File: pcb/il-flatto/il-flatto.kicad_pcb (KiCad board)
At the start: 2 copper layers, 88.3 x 63.5 mm, 52 parts, among them IC1 ATmega1284P-P, IC2 MCP1825S, IC3 MAX1811, Q1 12MHz, X2 SD_Card

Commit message: good to go?
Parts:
- removed - +: BAT, Connector_JST:JST_PH_B2B-PH-K_1x02_P2.00mm_Vertical
- removed the ? at (228.0, 128.3)
- removed the ? at (148.6, 128.3)
- removed the ? at (148.6, 73.7)
- removed the C1 at (176.5, 111.8)
- removed the C2 at (176.5, 95.2)
- removed the C3 at (168.9, 91.4)
- removed the C4 at (158.7, 89.5)
- removed the C5 at (174.0, 82.5)
- removed the C6 at (174.0, 89.5)
- removed the D1 at (165.7, 118.1)
- removed the G*** at (193.5, 101.0)
- removed the G*** at (188.1, 100.8)
- removed ISP: ISP, footprints:PinSocket_2x03_P2.54mm zero footprint mirror
- removed JTAG: JTAG, footprints:PinSocket_2x05_P2.54mm zero footprint mirror
- removed the Q1 at (175.3, 101.1)
- removed the R1 at (160.7, 99.7)
- removed the R10 at (209.6, 120.7)
- removed the R11 at (200.7, 117.5)
- removed the R2 at (170.8, 103.5)
- removed the R3 at (170.8, 107.3)
- removed the R4 at (170.8, 111.1)
- removed the R5 at (160.7, 95.9)
- removed the R6 at (219.7, 81.3)
- removed the R7 at (200.7, 84.5)
- removed the R8 at (218.4, 117.5)
- removed the R9 at (228.6, 84.5)
- removed the REF** at (228.0, 73.7)
- removed Reset: SW_SPST, Button_Switch_THT:SW_PUSH_6mm
- removed the SV1(A)1 at (216.5, 74.9)
- removed the SV2(B)1 at (170.2, 75.0)
- removed the SV3(C)1 at (205.8, 127.0)
- removed the SV4(D)1 at (160.1, 127.0)
- removed Se100: S1, footprints:EG1218
- added ?: , , F.Cu at (242.6, 83.3)
- added ?: , , F.Cu at (242.6, 154.3)
- added ?: , , F.Cu at (163.2, 28.6)
- added ?: , , F.Cu at (163.2, 99.7)
- added ?: , , F.Cu at (163.2, 154.3)
- added ?: , , F.Cu at (163.2, 83.3)
- added ?: ATmega1284P-P, Package_DIP:DIP-40_W15.24mm, F.Cu at (195.2, 102.8)
- added C1: 22pf, Capacitor_THT:C_Disc_D3.8mm_W2.6mm_P2.50mm, F.Cu at (191.1, 137.8)
- added C1: 22pf, Capacitor_THT:C_Disc_D3.8mm_W2.6mm_P2.50mm, F.Cu at (191.1, 66.7)
- added C101: 22pf, Capacitor_SMD:C_0402_1005Metric, F.Cu at (192.3, 132.3)
- added C102: 22pf, Capacitor_SMD:C_0402_1005Metric, F.Cu at (192.4, 126.9)
- added C103: 100nf, Capacitor_SMD:C_0402_1005Metric, F.Cu at (193.5, 125.0)
- added C104: 10uf, Capacitor_SMD:C_0402_1005Metric, F.Cu at (172.3, 117.5)
- added C105: 10uf, Capacitor_SMD:C_0402_1005Metric, F.Cu at (189.6, 110.5)
- added C106: 10uf, Capacitor_SMD:C_0402_1005Metric, F.Cu at (189.9, 113.7)
- added C107: 10uf, Capacitor_SMD:C_0402_1005Metric, F.Cu at (217.8, 99.7)
- added C108: 10uf, Capacitor_SMD:C_0402_1005Metric, F.Cu at (170.8, 99.7)
- added C109: 10uf, Capacitor_SMD:C_0402_1005Metric, F.Cu at (234.3, 154.3)
- added C110: 10uf, Capacitor_SMD:C_0402_1005Metric, F.Cu at (188.6, 154.3)
- added C111: 100nf, Capacitor_SMD:C_0402_1005Metric, F.Cu at (216.6, 99.7)
- added C112: 100nf, Capacitor_SMD:C_0402_1005Metric, F.Cu at (172.1, 99.7)
- added C113: 100nf, Capacitor_SMD:C_0402_1005Metric, F.Cu at (187.3, 154.3)
- added C114: 100nf, Capacitor_SMD:C_0402_1005Metric, F.Cu at (233.0, 154.3)
- added C2: 22pf, Capacitor_THT:C_Disc_D3.8mm_W2.6mm_P2.50mm, F.Cu at (191.1, 121.3)
- added C2: 22pf, Capacitor_THT:C_Disc_D3.8mm_W2.6mm_P2.50mm, F.Cu at (191.1, 50.2)
- added C205: 100nf, Capacitor_SMD:C_0402_1005Metric, F.Cu at (209.0, 126.8)
- added C206: 100nf, Capacitor_SMD:C_0402_1005Metric, F.Cu at (209.0, 124.8)
- added C3: 100nf, Capacitor_THT:C_Disc_D7.0mm_W2.5mm_P5.00mm, F.Cu at (183.5, 46.4)
- added C3: 100nf, Capacitor_THT:C_Disc_D7.0mm_W2.5mm_P5.00mm, F.Cu at (183.5, 117.5)
- added C300: 10u, Capacitor_SMD:C_0603_1608Metric, F.Cu at (241.7, 141.0)
- added C301: 10u, Capacitor_SMD:C_0603_1608Metric, F.Cu at (217.8, 137.0)
- added C302: 10u, Capacitor_SMD:C_0603_1608Metric, F.Cu at (241.7, 132.8)
- added C303: 10u, Capacitor_SMD:C_0603_1608Metric, F.Cu at (217.8, 128.9)
- added C304: 10u, Capacitor_SMD:C_0603_1608Metric, F.Cu at (241.7, 124.9)
- added C305: 10u, Capacitor_SMD:C_0603_1608Metric, F.Cu at (217.8, 121.0)
- added C306: 10u, Capacitor_SMD:C_0603_1608Metric, F.Cu at (241.7, 116.9)
- added C307: 10u, Capacitor_SMD:C_0603_1608Metric, F.Cu at (217.8, 112.9)
- added C4: 10uf, Capacitor_THT:CP_Radial_D5.0mm_P2.00mm, F.Cu at (173.3, 115.6)
- added C4: 10uf, Capacitor_THT:CP_Radial_D5.0mm_P2.00mm, F.Cu at (173.3, 44.5)
- added C5: 10uf, Capacitor_THT:CP_Radial_D5.0mm_P2.00mm, F.Cu at (188.6, 108.6)
- added C5: 10uf, Capacitor_THT:CP_Radial_D5.0mm_P2.00mm, F.Cu at (188.6, 37.5)
- added C6: 100uf, Capacitor_THT:CP_Radial_D5.0mm_P2.00mm, F.Cu at (188.6, 44.5)
- added C6: 100uf, Capacitor_THT:CP_Radial_D5.0mm_P2.00mm, F.Cu at (188.6, 115.6)
- added D1: LED, LED_THT:LED_D3.0mm, F.Cu at (180.3, 73.1)
- added D1: LED, LED_THT:LED_D3.0mm, F.Cu at (180.3, 144.1)
- added D101: LED, LED_SMD:LED_0603_1608Metric, F.Cu at (181.6, 142.2)
- added D102: CHRG, LED_SMD:LED_0603_1608Metric, F.Cu at (168.9, 117.5)
- added D200: SMD-LX0707RGB-TR, footprints:SMD-LX0707RGB-TR, F.Cu at (215.7, 141.0)
- added D201: SMD-LX0707RGB-TR, footprints:SMD-LX0707RGB-TR, F.Cu at (219.7, 141.0)
- added D202: SMD-LX0707RGB-TR, footprints:SMD-LX0707RGB-TR, F.Cu at (223.7, 141.0)
- added D203: SMD-LX0707RGB-TR, footprints:SMD-LX0707RGB-TR, F.Cu at (227.7, 141.0)
- added D204: SMD-LX0707RGB-TR, footprints:SMD-LX0707RGB-TR, F.Cu at (231.7, 141.0)
- added D205: SMD-LX0707RGB-TR, footprints:SMD-LX0707RGB-TR, F.Cu at (235.7, 141.0)
- added D206: SMD-LX0707RGB-TR, footprints:SMD-LX0707RGB-TR, F.Cu at (239.7, 141.0)
- added D207: SMD-LX0707RGB-TR, footprints:SMD-LX0707RGB-TR, F.Cu at (243.7, 141.0)
- added D208: SMD-LX0707RGB-TR, footprints:SMD-LX0707RGB-TR, F.Cu at (243.7, 137.0)
- added D209: SMD-LX0707RGB-TR, footprints:SMD-LX0707RGB-TR, F.Cu at (239.7, 137.0)
- added D210: SMD-LX0707RGB-TR, footprints:SMD-LX0707RGB-TR, F.Cu at (235.7, 137.0)
- added D211: SMD-LX0707RGB-TR, footprints:SMD-LX0707RGB-TR, F.Cu at (231.7, 137.0)
- added D212: SMD-LX0707RGB-TR, footprints:SMD-LX0707RGB-TR, F.Cu at (227.7, 137.0)
- added D213: SMD-LX0707RGB-TR, footprints:SMD-LX0707RGB-TR, F.Cu at (223.7, 137.0)
- added D214: SMD-LX0707RGB-TR, footprints:SMD-LX0707RGB-TR, F.Cu at (219.7, 137.0)
- added D215: SMD-LX0707RGB-TR, footprints:SMD-LX0707RGB-TR, F.Cu at (215.7, 137.0)
- added D216: SMD-LX0707RGB-TR, footprints:SMD-LX0707RGB-TR, F.Cu at (215.7, 133.0)
- added D217: SMD-LX0707RGB-TR, footprints:SMD-LX0707RGB-TR, F.Cu at (219.7, 133.0)
- added D218: SMD-LX0707RGB-TR, footprints:SMD-LX0707RGB-TR, F.Cu at (223.7, 133.0)
- added D219: SMD-LX0707RGB-TR, footprints:SMD-LX0707RGB-TR, F.Cu at (227.7, 133.0)
- added D220: SMD-LX0707RGB-TR, footprints:SMD-LX0707RGB-TR, F.Cu at (231.7, 133.0)
- added D221: SMD-LX0707RGB-TR, footprints:SMD-LX0707RGB-TR, F.Cu at (235.7, 133.0)
- added D222: SMD-LX0707RGB-TR, footprints:SMD-LX0707RGB-TR, F.Cu at (239.7, 133.0)
- added D223: SMD-LX0707RGB-TR, footprints:SMD-LX0707RGB-TR, F.Cu at (243.7, 133.0)
- added D224: SMD-LX0707RGB-TR, footprints:SMD-LX0707RGB-TR, F.Cu at (243.7, 129.0)
- added D225: SMD-LX0707RGB-TR, footprints:SMD-LX0707RGB-TR, F.Cu at (239.7, 129.0)
- added D226: SMD-LX0707RGB-TR, footprints:SMD-LX0707RGB-TR, F.Cu at (235.7, 129.0)
- added D227: SMD-LX0707RGB-TR, footprints:SMD-LX0707RGB-TR, F.Cu at (231.7, 129.0)
- added D228: SMD-LX0707RGB-TR, footprints:SMD-LX0707RGB-TR, F.Cu at (227.7, 129.0)
- added D229: SMD-LX0707RGB-TR, footprints:SMD-LX0707RGB-TR, F.Cu at (223.7, 129.0)
- added D230: SMD-LX0707RGB-TR, footprints:SMD-LX0707RGB-TR, F.Cu at (219.7, 129.0)
- added D231: SMD-LX0707RGB-TR, footprints:SMD-LX0707RGB-TR, F.Cu at (215.7, 129.0)
- added D232: SMD-LX0707RGB-TR, footprints:SMD-LX0707RGB-TR, F.Cu at (215.7, 125.0)
- added D233: SMD-LX0707RGB-TR, footprints:SMD-LX0707RGB-TR, F.Cu at (219.7, 125.0)
- added D234: SMD-LX0707RGB-TR, footprints:SMD-LX0707RGB-TR, F.Cu at (223.7, 125.0)
- added D235: SMD-LX0707RGB-TR, footprints:SMD-LX0707RGB-TR, F.Cu at (227.7, 125.0)
- added D236: SMD-LX0707RGB-TR, footprints:SMD-LX0707RGB-TR, F.Cu at (231.7, 125.0)
- added D237: SMD-LX0707RGB-TR, footprints:SMD-LX0707RGB-TR, F.Cu at (235.7, 125.0)
- added D238: SMD-LX0707RGB-TR, footprints:SMD-LX0707RGB-TR, F.Cu at (239.7, 125.0)
- added D239: SMD-LX0707RGB-TR, footprints:SMD-LX0707RGB-TR, F.Cu at (243.7, 125.0)
- added D240: SMD-LX0707RGB-TR, footprints:SMD-LX0707RGB-TR, F.Cu at (243.7, 121.0)
- added D241: SMD-LX0707RGB-TR, footprints:SMD-LX0707RGB-TR, F.Cu at (239.7, 121.0)
- added D242: SMD-LX0707RGB-TR, footprints:SMD-LX0707RGB-TR, F.Cu at (235.7, 121.0)
- added D243: SMD-LX0707RGB-TR, footprints:SMD-LX0707RGB-TR, F.Cu at (231.7, 121.0)
- added D244: SMD-LX0707RGB-TR, footprints:SMD-LX0707RGB-TR, F.Cu at (227.7, 121.0)
- added D245: SMD-LX0707RGB-TR, footprints:SMD-LX0707RGB-TR, F.Cu at (223.7, 121.0)
- added D246: SMD-LX0707RGB-TR, footprints:SMD-LX0707RGB-TR, F.Cu at (219.7, 121.0)
- added D247: SMD-LX0707RGB-TR, footprints:SMD-LX0707RGB-TR, F.Cu at (215.7, 121.0)
- added D248: SMD-LX0707RGB-TR, footprints:SMD-LX0707RGB-TR, F.Cu at (215.7, 117.0)
- added D249: SMD-LX0707RGB-TR, footprints:SMD-LX0707RGB-TR, F.Cu at (219.7, 117.0)
- added D250: SMD-LX0707RGB-TR, footprints:SMD-LX0707RGB-TR, F.Cu at (223.7, 117.0)
- added D251: SMD-LX0707RGB-TR, footprints:SMD-LX0707RGB-TR, F.Cu at (227.7, 117.0)
- added D252: SMD-LX0707RGB-TR, footprints:SMD-LX0707RGB-TR, F.Cu at (231.7, 117.0)
- added D253: SMD-LX0707RGB-TR, footprints:SMD-LX0707RGB-TR, F.Cu at (235.7, 117.0)
- added D254: SMD-LX0707RGB-TR, footprints:SMD-LX0707RGB-TR, F.Cu at (239.7, 117.0)
- added D255: SMD-LX0707RGB-TR, footprints:SMD-LX0707RGB-TR, F.Cu at (243.7, 117.0)
- added D256: SMD-LX0707RGB-TR, footprints:SMD-LX0707RGB-TR, F.Cu at (243.7, 113.0)
- added D257: SMD-LX0707RGB-TR, footprints:SMD-LX0707RGB-TR, F.Cu at (239.7, 113.0)
- added D258: SMD-LX0707RGB-TR, footprints:SMD-LX0707RGB-TR, F.Cu at (235.7, 113.0)
- added D259: SMD-LX0707RGB-TR, footprints:SMD-LX0707RGB-TR, F.Cu at (231.7, 113.0)
- added D260: SMD-LX0707RGB-TR, footprints:SMD-LX0707RGB-TR, F.Cu at (227.7, 113.0)
- added D261: SMD-LX0707RGB-TR, footprints:SMD-LX0707RGB-TR, F.Cu at (223.7, 113.0)
- added D262: SMD-LX0707RGB-TR, footprints:SMD-LX0707RGB-TR, F.Cu at (219.7, 113.0)
- added D263: SMD-LX0707RGB-TR, footprints:SMD-LX0707RGB-TR, F.Cu at (215.7, 113.0)
- added J103: ISP, footprints:PinSocket_2x03_P2.54mm zero footprint mirror, F.Cu at (162.1, 113.7)
- added J105: JTAG, footprints:PinSocket_2x05_P2.54mm zero footprint mirror, F.Cu at (161.9, 145.4)
- added J3: ISP, footprints:PinSocket_2x03_P2.54mm zero footprint mirror, F.Cu at (162.1, 42.6)
- added J5: JTAG, footprints:PinSocket_2x05_P2.54mm zero footprint mirror, F.Cu at (161.9, 74.4)
- added JP103: Conn_01x03, footprints:PinHeader_1x03_P2.54mm zero footprint, F.Cu at (190.5, 146.7)
- added Q1: 12MHz, Crystal:Crystal_HC49-4H_Vertical, F.Cu at (189.9, 127.1)
- added Q1: 12MHz, Crystal:Crystal_HC49-4H_Vertical, F.Cu at (189.9, 56.0)
- added Q101: 12MHz, Crystal:Crystal_SMD_Abracon_ABM8G-4Pin_3.2x2.5mm, F.Cu at (192.3, 129.6)
- added R1: 68, Resistor_THT:R_Axial_DIN0207_L6.3mm_D2.5mm_P10.16mm_Horizontal, F.Cu at (175.3, 125.7)
- added R1: 68, Resistor_THT:R_Axial_DIN0207_L6.3mm_D2.5mm_P10.16mm_Horizontal, F.Cu at (175.3, 54.7)
- added R10: 68, Resistor_THT:R_Axial_DIN0207_L6.3mm_D2.5mm_P10.16mm_Horizontal, F.Cu at (224.2, 146.7)
- added R10: 68, Resistor_THT:R_Axial_DIN0207_L6.3mm_D2.5mm_P10.16mm_Horizontal, F.Cu at (224.2, 75.6)
- added R101: 68, Resistor_SMD:R_0402_1005Metric, F.Cu at (180.3, 125.1)
- added R102: 68, Resistor_SMD:R_0402_1005Metric, F.Cu at (180.3, 126.4)
- added R103: 1.5k, Resistor_SMD:R_0402_1005Metric, F.Cu at (178.4, 135.3)
- added R104: 220, Resistor_SMD:R_0402_1005Metric, F.Cu at (181.6, 141.0)
- added R105: 10k, Resistor_SMD:R_0402_1005Metric, F.Cu at (178.4, 140.3)
- added R106: 68, Resistor_SMD:R_0402_1005Metric, F.Cu at (229.4, 107.3)
- added R107: 68, Resistor_SMD:R_0402_1005Metric, F.Cu at (220.5, 110.5)
- added R108: 68, Resistor_SMD:R_0402_1005Metric, F.Cu at (238.3, 143.5)
- added R109: 68, Resistor_SMD:R_0402_1005Metric, F.Cu at (238.2, 110.5)
- added R11: 68, Resistor_THT:R_Axial_DIN0207_L6.3mm_D2.5mm_P10.16mm_Horizontal, F.Cu at (215.3, 72.5)
- added R11: 68, Resistor_THT:R_Axial_DIN0207_L6.3mm_D2.5mm_P10.16mm_Horizontal, F.Cu at (215.3, 143.5)
- added R110: 68, Resistor_SMD:R_0402_1005Metric, F.Cu at (229.5, 146.7)
- added R111: 68, Resistor_SMD:R_0402_1005Metric, F.Cu at (220.5, 143.5)
- added R112: 470, Resistor_SMD:R_0402_1005Metric, F.Cu at (168.9, 114.9)
- added R2: 68, Resistor_THT:R_Axial_DIN0207_L6.3mm_D2.5mm_P10.16mm_Horizontal, F.Cu at (185.4, 129.5)
- added R2: 68, Resistor_THT:R_Axial_DIN0207_L6.3mm_D2.5mm_P10.16mm_Horizontal, F.Cu at (185.4, 58.5)
- added R201: 5.1k, Resistor_SMD:R_0402_1005Metric, F.Cu at (165.7, 117.5)
- added R202: 5.1k, Resistor_SMD:R_0402_1005Metric, F.Cu at (167.0, 132.1)
- added R203: 2.5k, Resistor_SMD:R_0402_1005Metric, F.Cu at (177.8, 132.7)
- added R204: 10k, Resistor_SMD:R_0402_1005Metric, F.Cu at (179.1, 132.7)
- added R3: 1.5k, Resistor_THT:R_Axial_DIN0207_L6.3mm_D2.5mm_P10.16mm_Horizontal, F.Cu at (185.4, 133.3)
- added R3: 1.5k, Resistor_THT:R_Axial_DIN0207_L6.3mm_D2.5mm_P10.16mm_Horizontal, F.Cu at (185.4, 62.3)
- added R4: 220, Resistor_THT:R_Axial_DIN0207_L6.3mm_D2.5mm_P10.16mm_Horizontal, F.Cu at (185.4, 137.2)
- added R4: 220, Resistor_THT:R_Axial_DIN0207_L6.3mm_D2.5mm_P10.16mm_Horizontal, F.Cu at (185.4, 66.1)
- added R5: 10k, Resistor_THT:R_Axial_DIN0207_L6.3mm_D2.5mm_P10.16mm_Horizontal, F.Cu at (175.3, 50.9)
- added R5: 10k, Resistor_THT:R_Axial_DIN0207_L6.3mm_D2.5mm_P10.16mm_Horizontal, F.Cu at (175.3, 121.9)
- added R6: 68, Resistor_THT:R_Axial_DIN0207_L6.3mm_D2.5mm_P10.16mm_Horizontal, F.Cu at (234.3, 36.3)
- added R6: 68, Resistor_THT:R_Axial_DIN0207_L6.3mm_D2.5mm_P10.16mm_Horizontal, F.Cu at (234.3, 107.3)
- added R7: 68, Resistor_THT:R_Axial_DIN0207_L6.3mm_D2.5mm_P10.16mm_Horizontal, F.Cu at (215.3, 110.5)
- added R7: 68, Resistor_THT:R_Axial_DIN0207_L6.3mm_D2.5mm_P10.16mm_Horizontal, F.Cu at (215.3, 39.4)
- added R8: 68, Resistor_THT:R_Axial_DIN0207_L6.3mm_D2.5mm_P10.16mm_Horizontal, F.Cu at (233.0, 72.5)
- added R8: 68, Resistor_THT:R_Axial_DIN0207_L6.3mm_D2.5mm_P10.16mm_Horizontal, F.Cu at (233.0, 143.5)
- added R9: 68, Resistor_THT:R_Axial_DIN0207_L6.3mm_D2.5mm_P10.16mm_Horizontal, F.Cu at (243.2, 39.4)
- added R9: 68, Resistor_THT:R_Axial_DIN0207_L6.3mm_D2.5mm_P10.16mm_Horizontal, F.Cu at (243.2, 110.5)
- added REF**: MountingHole_3mm_Pad, MountingHole:MountingHole_3mm_Pad, F.Cu at (242.6, 99.7)
- added REF**: MountingHole_3mm_Pad, MountingHole:MountingHole_3mm_Pad, F.Cu at (242.6, 28.6)
- added S1: S1, footprints:EG1218, F.Cu at (171.4, 61.0)
- added S1: S1, footprints:EG1218, F.Cu at (171.4, 132.0)
- added S101: PWR SEL, footprints:CS-4-12XA, F.Cu at (170.8, 121.3)
- added S102: SW_SPST, footprints:SW_TL3780AF240QG, F.Cu at (172.7, 143.7)
- added S103: SW_DPST_x2, footprints:CVS-02TB mirrored, F.Cu at (180.1, 129.5)
- added S2: SW_SPST, Button_Switch_THT:SW_PUSH_6mm, F.Cu at (176.0, 74.7)
- added S2: SW_SPST, Button_Switch_THT:SW_PUSH_6mm, F.Cu at (176.0, 145.8)
- added SV1(A)1: Conn_02x05_Odd_Even, footprints:PinSocket_2x05_P2.54mm zero footprint mirror, F.Cu at (230.5, 29.9)
- added SV1(A)1: Conn_02x05_Odd_Even, footprints:PinSocket_2x05_P2.54mm zero footprint mirror, F.Cu at (230.5, 101.0)
- added SV2(B)1: Conn_02x05_Odd_Even, footprints:PinSocket_2x05_P2.54mm zero footprint mirror, F.Cu at (184.8, 101.0)
- added SV2(B)1: Conn_02x05_Odd_Even, footprints:PinSocket_2x05_P2.54mm zero footprint mirror, F.Cu at (184.8, 29.9)
- added SV3(C)1: Conn_02x05_Odd_Even, footprints:PinSocket_2x05_P2.54mm zero footprint mirror, F.Cu at (220.4, 82.0)
- added SV3(C)1: Conn_02x05_Odd_Even, footprints:PinSocket_2x05_P2.54mm zero footprint mirror, F.Cu at (220.4, 153.0)
- added SV4(D)1: Conn_02x05_Odd_Even, footprints:PinSocket_2x05_P2.54mm zero footprint mirror, F.Cu at (174.7, 82.0)
- added SV4(D)1: Conn_02x05_Odd_Even, footprints:PinSocket_2x05_P2.54mm zero footprint mirror, F.Cu at (174.7, 153.0)
- added U101: ATmega1284P-M, Package_DFN_QFN:QFN-44-1EP_7x7mm_P0.5mm_EP5.2x5.2mm, F.Cu at (202.7, 125.8)
- added U102: NCV8605MN33T2G, footprints:NCV8605MN33T2G, F.Cu at (178.6, 114.2)
- added U103: MCP73831-2-MC, Package_DFN_QFN:DFN-8-1EP_3x2mm_P0.5mm_EP1.75x1.45mm, F.Cu at (171.4, 111.8)
- added X101: USB_C_Receptacle_USB2.0, footprints:GCT_USB4110-GF-A_REVB, F.Cu at (165.3, 124.8)
- added X102: SD_Card, footprints:sd card, F.Cu at (237.8, 127.0)
- added X103: BAT, Connector_JST:JST_PH_B2B-PH-K_1x02_P2.00mm_Vertical, F.Cu at (173.4, 108.6)
- added X3: BAT, Connector_JST:JST_PH_B2B-PH-K_1x02_P2.00mm_Vertical, F.Cu at (173.4, 37.5)
- S3: footprint footprints:SW_CAS-D20TA -> footprints:CAS-D20TB
- moved IC1 47.3 mm to (195.2, 31.8)
- moved IC2 47.3 mm to (181.0, 39.4)
- moved JP3 47.3 mm to (190.5, 75.6)
- moved X2 47.3 mm to (237.8, 56.0)
- moved C10 29.9 mm to (189.9, 154.3)
- moved C12 29.9 mm to (172.1, 99.7)
- moved C9 29.9 mm to (235.6, 154.3)
- moved D2 29.9 mm to (168.9, 118.7)
- moved IC3 29.9 mm to (179.7, 110.5)
- moved R12 29.9 mm to (174.6, 118.7)
- moved S3 29.9 mm to (179.7, 129.5)
- moved C13 29.9 mm to (187.3, 154.3)
- moved C14 29.9 mm to (233.0, 154.3)
- moved C8 29.9 mm to (169.5, 99.7)
- moved G*** 29.9 mm to (228.6, 127.0)
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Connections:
- IC2 pad 1: Net-(IC2-Pad1) -> LDO_in
- IC3 pad 5: /externals/V_BAT -> V_BAT
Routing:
- net VDD: track 297.4 -> 905.9 mm
- net PB0: track 81.4 -> 259.7 mm
- net PB1: track 73.6 -> 227.5 mm
- net PC3: track 70.8 -> 179.4 mm
- net PC5: track 138.4 -> 237.3 mm
- net GND: track 0.00 -> 91.9 mm
- net PB5: track 91.6 -> 178.8 mm
- net PC2: track 85.1 -> 171.3 mm
- net V_BAT: track 0.00 -> 82.9 mm
- net n_reset: track 80.1 -> 145.9 mm
- net PB2: track 47.9 -> 110.9 mm
- net PD7: track 30.1 -> 85.9 mm
- net PD0: track 37.7 -> 85.9 mm
- net PB3: track 59.6 -> 104.6 mm
- net Net-(R203-Pad1): track 0.00 -> 44.9 mm
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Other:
- board size 88.3 x 63.5 mm -> 88.3 x 134.6 mm
- board text added: "ISP"
- board text added: "JTAG"

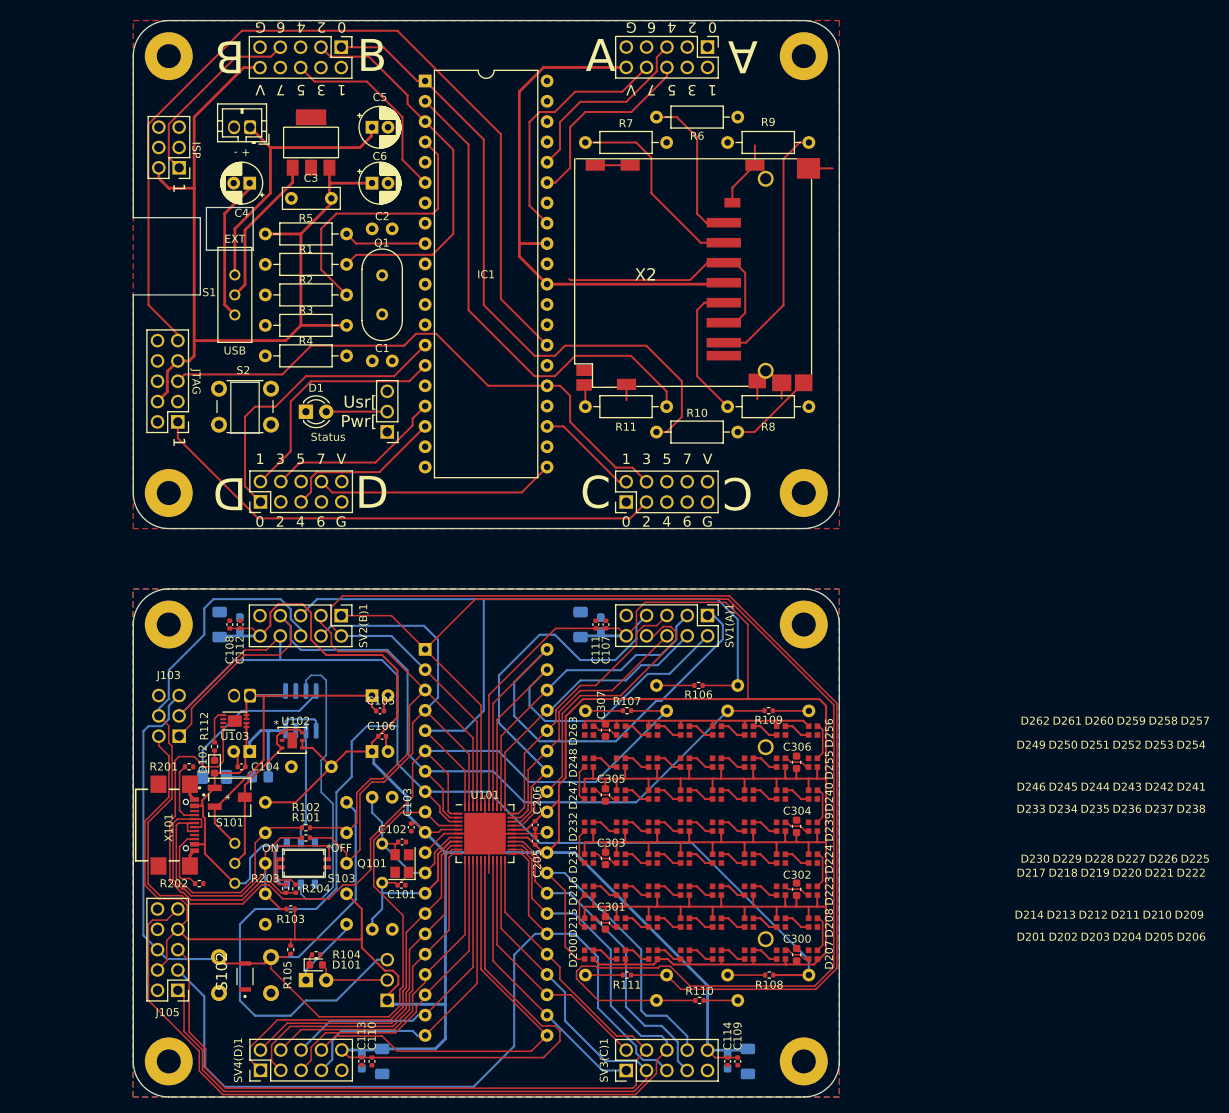
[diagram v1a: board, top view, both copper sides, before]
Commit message: changed to 1.5mm RGBLEDs because cheaper
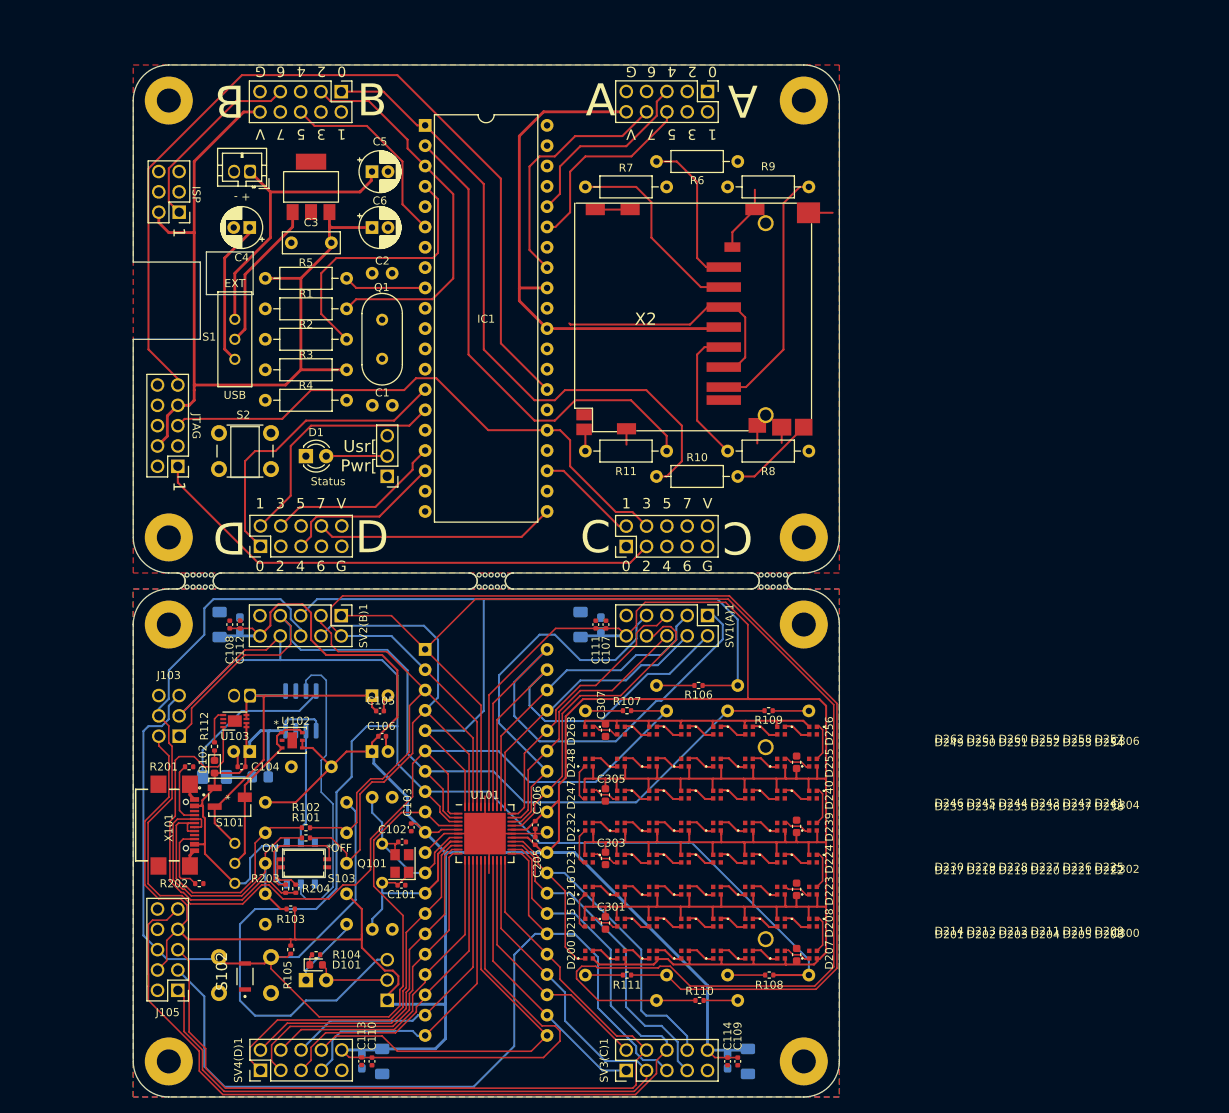
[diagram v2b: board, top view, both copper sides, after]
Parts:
- added mouse-bite-3mm-slot: VAL**, footprints:mouse-bite-3mm-slot, F.Cu at (238.8, 94.2)
- added mouse-bite-3mm-slot: VAL**, footprints:mouse-bite-3mm-slot, F.Cu at (203.5, 94.2)
- added mouse-bite-3mm-slot: VAL**, footprints:mouse-bite-3mm-slot, F.Cu at (167.0, 94.2)
- D200, D201, D202, D203, D204, D205, D206, D207, D208, D209, D210, D211, D212, D213, D214, D215, D216, D217, D218, D219, D220, D221, D222, D223, D224, D225, D226, D227, D228, D229, D230, D231, D232, D233, D234, D235, D236, D237, D238, D239, D240, D241, D242, D243, D244, D245, D246, D247, D248, D249, D250, D251, D252, D253, D254, D255, D256, D257, D258, D259, D260, D261, D262, D263: value SMD-LX0707RGB-TR -> IN-PI15TAT5R5G5B; footprint footprints:SMD-LX0707RGB-TR -> footprints:INPI15TAT5R5G5B
- moved ? 5.55 mm to (242.6, 88.8)
- moved ? 5.55 mm to (163.2, 88.8)
- moved J5 5.55 mm to (161.9, 79.9)
- moved R11 5.55 mm to (215.3, 78.0)
- moved R8 5.55 mm to (233.0, 78.0)
- moved S2 5.55 mm to (176.0, 80.3)
- moved C3 5.55 mm to (183.5, 52.0)
- moved C5 5.55 mm to (188.6, 43.1)
- moved IC2 5.55 mm to (181.0, 45.0)
- moved Q1 5.55 mm to (189.9, 61.6)
- moved R2 5.55 mm to (185.4, 64.0)
- moved R5 5.55 mm to (175.3, 56.4)
- moved R7 5.55 mm to (215.3, 45.0)
- moved R9 5.55 mm to (243.2, 45.0)
- moved S1 5.55 mm to (171.4, 66.5)
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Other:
- board size 88.3 x 134.6 mm -> 88.3 x 129 mm

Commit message: messing around
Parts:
- added G***: LOGO, footprints:text, B.Cu at (241.0, 106.2)
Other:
- board text added: "Alexander Mills, 2023, Rev A"
- board text added: "Il-Flatto"
